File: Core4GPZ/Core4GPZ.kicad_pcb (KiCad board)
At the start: 2 copper layers, 88.9 x 114.3 mm, 20 parts, among them Q1 IRG4PF50W, Q2 IRG4PF50W, U1 core4, U2 MPX4250

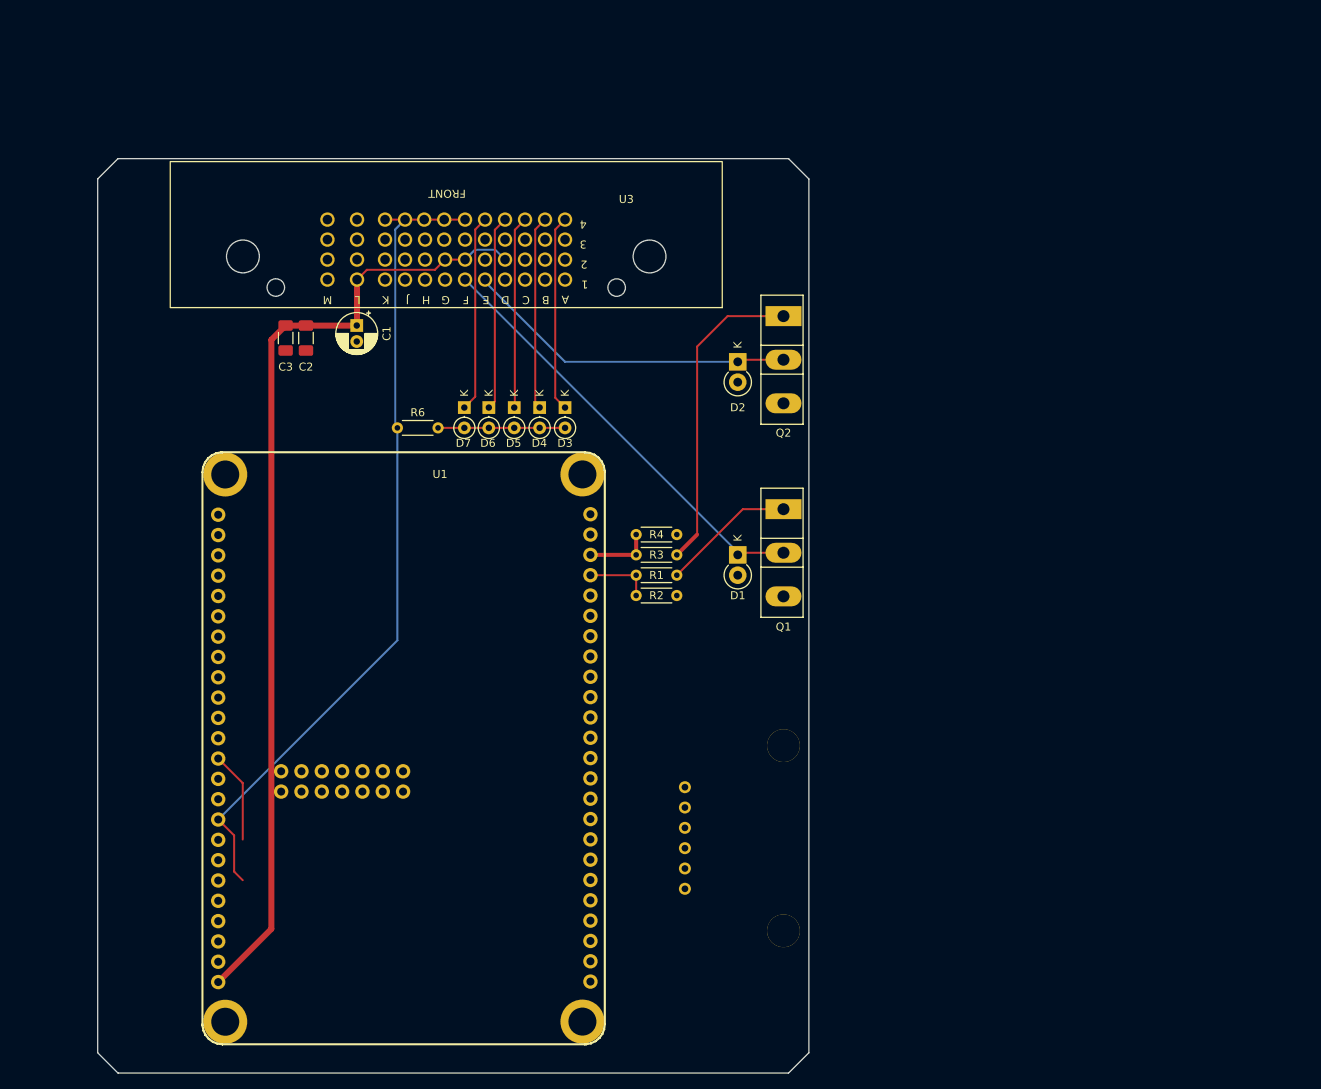
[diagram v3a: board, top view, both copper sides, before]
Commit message: Started Implementation of VR Conditionner
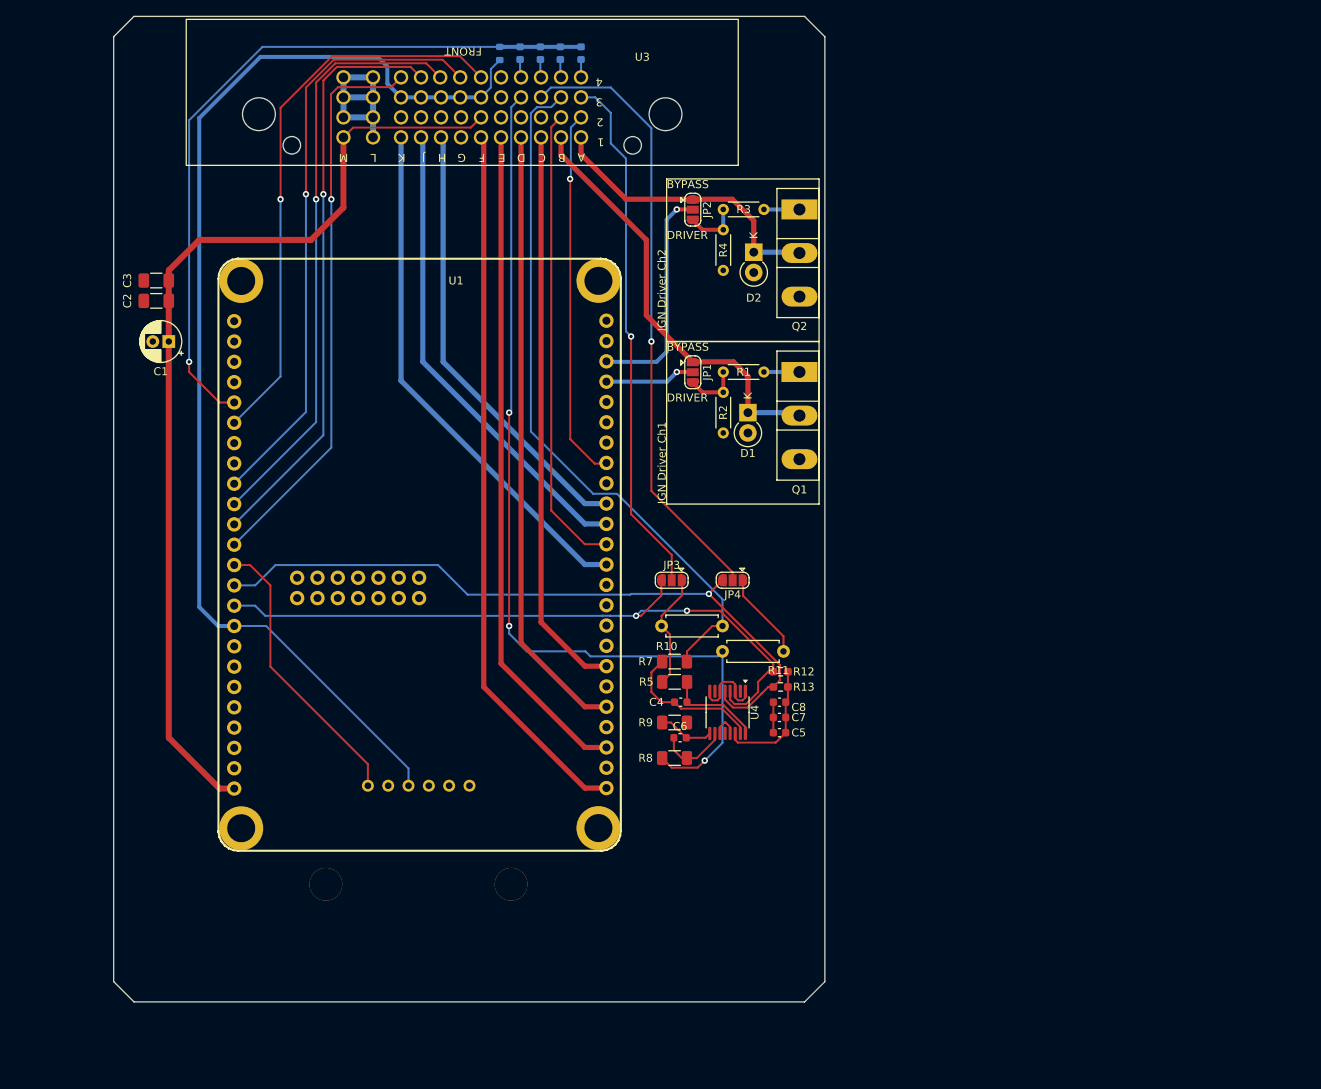
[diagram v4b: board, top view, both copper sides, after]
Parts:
- removed D7: D, Diode_THT:D_DO-35_SOD27_P2.54mm_Vertical_KathodeUp
- added C4: 1n, Capacitor_SMD:C_0603_1608Metric, F.Cu at (126.2, 108.6)
- added C5: 10n, Capacitor_SMD:C_0603_1608Metric, F.Cu at (138.6, 112.4)
- added C6: 1n, Capacitor_SMD:C_0603_1608Metric, F.Cu at (126.1, 113.0)
- added C7: 100n, Capacitor_SMD:C_0603_1608Metric, F.Cu at (138.6, 110.5)
- added C8: 1u, Capacitor_SMD:C_0603_1608Metric, F.Cu at (138.6, 108.6)
- added JP1: SolderJumper_3_Open, Jumper:SolderJumper-3_P1.3mm_Open_RoundedPad1.0x1.5mm, F.Cu at (127.7, 67.3)
- added JP2: SolderJumper_3_Open, Jumper:SolderJumper-3_P1.3mm_Open_RoundedPad1.0x1.5mm, F.Cu at (127.7, 47.0)
- added JP3: Crank - VR/Hall Selector, Jumper:SolderJumper-3_P1.3mm_Open_RoundedPad1.0x1.5mm, F.Cu at (125.1, 93.3)
- added JP4: Cam - VR/Hall Selector, Jumper:SolderJumper-3_P1.3mm_Open_RoundedPad1.0x1.5mm, F.Cu at (132.7, 93.3)
- added R10: 4.7k, Resistor_THT:R_Axial_DIN0207_L6.3mm_D2.5mm_P7.62mm_Horizontal, F.Cu at (123.8, 99.1)
- added R11: 4.7k, Resistor_THT:R_Axial_DIN0207_L6.3mm_D2.5mm_P7.62mm_Horizontal, F.Cu at (139.1, 102.2)
- added R12: 1k, Resistor_SMD:R_0603_1608Metric_Pad0.98x0.95mm_HandSolder, F.Cu at (138.7, 104.8)
- added R13: 1k, Resistor_SMD:R_0603_1608Metric_Pad0.98x0.95mm_HandSolder, F.Cu at (138.7, 106.7)
- added R5: 10k, Resistor_SMD:R_1206_3216Metric_Pad1.30x1.75mm_HandSolder, F.Cu at (125.5, 106.0)
- added R7: 10k, Resistor_SMD:R_1206_3216Metric_Pad1.30x1.75mm_HandSolder, F.Cu at (125.5, 103.5)
- added R8: 10k, Resistor_SMD:R_1206_3216Metric_Pad1.30x1.75mm_HandSolder, F.Cu at (125.5, 115.6)
- added R9: 10k, Resistor_SMD:R_1206_3216Metric_Pad1.30x1.75mm_HandSolder, F.Cu at (125.5, 111.1)
- added U4: MAX9926UAEE+, Package_SO:QSOP-16_3.9x4.9mm_P0.635mm, F.Cu at (132.1, 109.9)
- D3, D4, D5, D6: footprint Diode_THT:D_DO-35_SOD27_P2.54mm_Vertical_KathodeUp -> Diode_SMD:D_0603_1608Metric; moved to B.Cu
- R6: footprint Resistor_THT:R_Axial_DIN0204_L3.6mm_D1.6mm_P5.08mm_Horizontal -> Resistor_SMD:R_0603_1608Metric; moved to B.Cu
- moved R6 48.5 mm to (103.6, 27.5), turned to 90 degrees
- moved R3 44.5 mm to (136.6, 47.0)
- moved D6 44.5 mm to (106.1, 27.5), turned to 90 degrees
- moved D5 44.4 mm to (108.7, 27.5), turned to 90 degrees
- moved D4 44.4 mm to (111.2, 27.5), turned to 90 degrees
- moved D3 44.3 mm to (113.8, 27.5), turned to 90 degrees
- moved U2 41.7 mm to (87.1, 119.0), turned to 0 degrees
- moved R4 39.6 mm to (131.5, 49.5), turned to -90 degrees
- moved R2 27.6 mm to (131.5, 69.8), turned to -90 degrees
- moved R1 27.6 mm to (136.6, 67.3)
- moved U1 24.3 mm to (116.9, 119.3)
- moved C1 23.6 mm to (62.2, 63.5), turned to 180 degrees
- moved C2 19.3 mm to (60.7, 58.4), turned to 180 degrees
- moved U3 17.9 mm to (98.9, 22.8)
- moved D1 17.8 mm to (134.6, 72.4)
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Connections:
- R1 pad 2: IGN_TRIG_1 -> Net-(JP1-B)
- R2 pad 1: IGN_TRIG_1 -> Net-(JP1-B)
- R3 pad 2: IGN_TRIG_2 -> Net-(JP2-B)
- R4 pad 1: IGN_TRIG_2 -> Net-(JP2-B)
- U1 pad 34: /CRANK_SNSR -> CRANK_SIGNAL
- U1 pad 35: /CAM_SNSR -> CAM_SIGNAL
- U1 pad 40: /O2_SNSR -> /02_SNSR
- U1 pad 61: BIKE_+12V_SWITCHED_IN -> BIKE_GROUND
- U1 pad 62: BIKE_+12V_SWITCHED_IN -> unconnected-(U1C-+5V-Pad62)
- U3 pad 1: /INJ1_TRIG -> IGN_COIL2_DRIVE
- U3 pad 10: unconnected-(U3A-1K-Pad10) -> /IDLE_1
- U3 pad 11: BIKE_+12V_SWITCHED_IN -> /NEUTRAL_LIGHT
- U3 pad 14: BIKE_+12V_SWITCHED_IN -> unconnected-(U3A-2D-Pad14)
- U3 pad 15: /NEUTRAL_LIGHT -> unconnected-(U3A-2E-Pad15)
- U3 pad 17: BIKE_+12V_SWITCHED_IN -> unconnected-(U3A-2G-Pad17)
- U3 pad 18: /FAN_CTL -> unconnected-(U3A-2H-Pad18)
- U3 pad 19: /IDLE_1 -> unconnected-(U3A-2J-Pad19)
- U3 pad 2: /INJ2_TRIG -> IGN_COIL1_DRIVE
- U3 pad 20: /FUEL_PUMP -> unconnected-(U3A-2K-Pad20)
- U3 pad 21: /CRANK_SNSR -> CRANK_SNSR
- U3 pad 22: /CAM_SNSR -> CRANK_SNSR_VR-
- U3 pad 23: unconnected-(U3B-3C-Pad23) -> CAM_SNSR
- U3 pad 24: unconnected-(U3B-3D-Pad24) -> CAM_SNSR_VR-
- U3 pad 26: /FLEX_SNSR -> CLT_+5V
- U3 pad 27: /02_SNSR -> CLT_+5V
- U3 pad 28: /IAT_SNSR -> CLT_+5V
- U3 pad 29: /CLT_SNSR -> CLT_+5V
- U3 pad 3: /INJ3_TRIG -> /INJ4_TRIG
- U3 pad 30: /TPS_SNSR -> CLT_+5V
- U3 pad 36: CLT_+5V -> /FLEX_SNSR
- U3 pad 37: CLT_+5V -> /02_SNSR
- U3 pad 38: CLT_+5V -> /IAT_SNSR
- U3 pad 39: CLT_+5V -> /CLT_SNSR
- U3 pad 4: /INJ4_TRIG -> /INJ3_TRIG
- U3 pad 40: CLT_+5V -> /TPS_SNSR
- U3 pad 41: BIKE_+12V_SWITCHED_IN -> BIKE_GROUND
- U3 pad 42: BIKE_GROUND -> BIKE_+12V_SWITCHED_IN
- U3 pad 5: IGN_COIL2_DRIVE -> /INJ2_TRIG
- U3 pad 6: IGN_COIL1_DRIVE -> /INJ1_TRIG
- U3 pad 8: unconnected-(U3A-1H-Pad8) -> /FAN_CTL
- U3 pad 9: unconnected-(U3A-1J-Pad9) -> /FUEL_PUMP
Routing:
- net CAM_SNSR_VR-: track 0.00 -> 116.5 mm, vias 0 -> 3
- net /INJ1_TRIG: track 0.00 -> 89.4 mm
- net CAM_SIGNAL: track 0.00 -> 89.1 mm, vias 0 -> 1
- net CRANK_SNSR_VR-: track 0.00 -> 87.4 mm
- net CRANK_SIGNAL: track 0.00 -> 87.1 mm, vias 0 -> 2
- net /INJ2_TRIG: track 0.00 -> 83.6 mm
- net /INJ3_TRIG: track 0.00 -> 77.2 mm
- net CAM_SNSR: track 0.00 -> 77.1 mm, vias 0 -> 1
- net SAFE_SIGNAL: track 15.9 -> 92.0 mm, vias 0 -> 1
- net /02_SNSR: track 0.00 -> 74.9 mm, vias 0 -> 1
- net /IAT_SNSR: track 0.00 -> 74.2 mm, vias 0 -> 1
- net /CLT_SNSR: track 0.00 -> 73.6 mm, vias 0 -> 1
- net /INJ4_TRIG: track 0.00 -> 71.1 mm
- net /TPS_SNSR: track 0.00 -> 71.0 mm, vias 0 -> 1
- net /FLEX_SNSR: track 0.00 -> 70.6 mm, vias 0 -> 1
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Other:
- board size 88.9 x 114.3 mm -> 88.9 x 123.2 mm
- board text added: "BYPASS"
- board text added: "DRIVER"
- board text added: "IGN Driver Ch1"
- board text added: "IGN Driver Ch2"

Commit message: Implemented VR_Conditionner (MAX9926+)
First look at ground plane
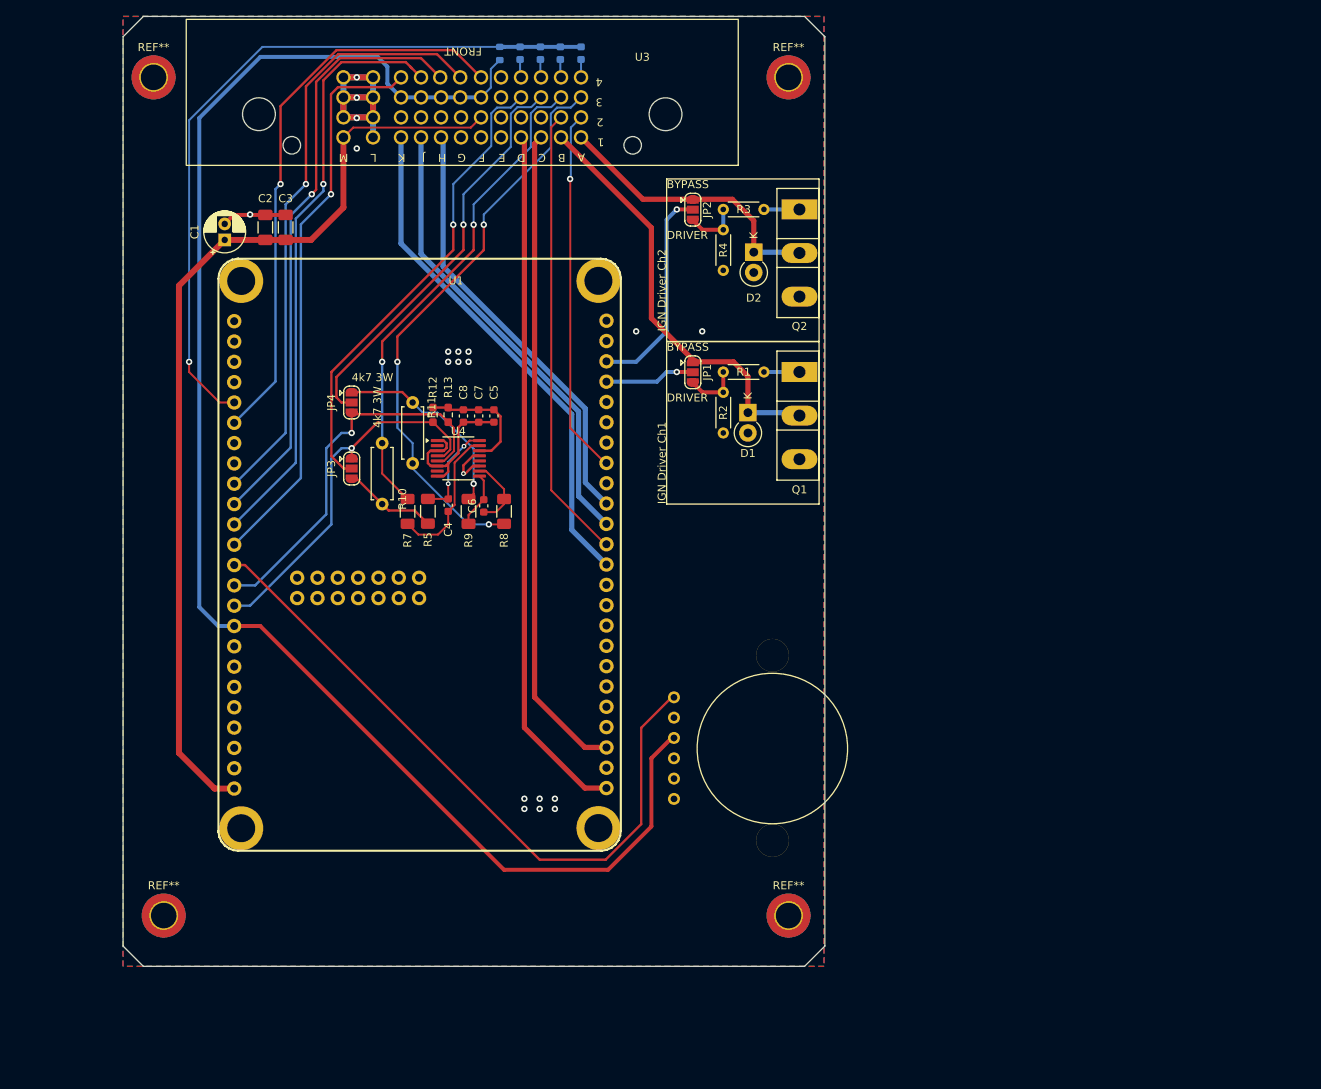
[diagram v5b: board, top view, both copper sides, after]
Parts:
- added REF**: MountingHole_3.2mm_M3_ISO14580_Pad_TopBottom, MountingHole:MountingHole_3.2mm_M3_ISO14580_Pad_TopBottom, F.Cu at (61.6, 135.3)
- added REF**: MountingHole_3.2mm_M3_ISO14580_Pad_TopBottom, MountingHole:MountingHole_3.2mm_M3_ISO14580_Pad_TopBottom, F.Cu at (139.7, 30.5)
- added REF**: MountingHole_3.2mm_M3_ISO14580_Pad_TopBottom, MountingHole:MountingHole_3.2mm_M3_ISO14580_Pad_TopBottom, F.Cu at (60.3, 30.5)
- added REF**: MountingHole_3.2mm_M3_ISO14580_Pad_TopBottom, MountingHole:MountingHole_3.2mm_M3_ISO14580_Pad_TopBottom, F.Cu at (139.7, 135.3)
- U2: moved to F.Cu
- moved R11 55.8 mm to (92.7, 71.1), turned to -90 degrees
- moved R12 54.0 mm to (95.2, 72.7), turned to -90 degrees
- moved R13 53.7 mm to (97.2, 72.7), turned to -90 degrees
- moved C5 53.3 mm to (102.9, 72.8), turned to -90 degrees
- moved C8 53.3 mm to (99.1, 72.8), turned to -90 degrees
- moved C7 53.2 mm to (101.0, 72.8), turned to -90 degrees
- moved JP4 52.6 mm to (85.1, 71.1), turned to -90 degrees
- moved U4 46.3 mm to (98.4, 78.1), turned to 0 degrees
- moved JP3 42.4 mm to (85.1, 79.4), turned to -90 degrees
- moved U2 39.8 mm to (125.4, 108.0), turned to -90 degrees
- moved R7 38.3 mm to (92.1, 84.7), turned to 90 degrees
- moved R10 38.1 mm to (88.9, 83.8), turned to 90 degrees
- moved C4 38.1 mm to (97.2, 84.0), turned to -90 degrees
- moved C6 38.0 mm to (101.6, 84.0), turned to 90 degrees
- moved R5 37.5 mm to (94.6, 84.7), turned to -90 degrees
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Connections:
- JP3 pad 1: Net-(JP3-A) -> CRANK_SIGNAL
- JP3 pad 3: CRANK_SIGNAL -> Net-(JP3-B)
- R10 pad 1: Net-(JP3-A) -> Net-(JP3-B)
- R5 pad 2: Net-(JP3-A) -> Net-(JP3-B)
- U3 pad 21: CRANK_SNSR -> CAM_SNSR_VR-
- U3 pad 24: CAM_SNSR_VR- -> CRANK_SNSR
- U3 pad 3: /INJ4_TRIG -> /INJ2_TRIG
- U3 pad 4: /INJ3_TRIG -> /INJ1_TRIG
- U3 pad 5: /INJ2_TRIG -> unconnected-(U3A-1E-Pad5)
- U3 pad 6: /INJ1_TRIG -> unconnected-(U3A-1F-Pad6)
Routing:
- net /INJ3_TRIG: track 77.2 -> 0.00 mm
- net /INJ4_TRIG: track 71.1 -> 0.00 mm
- net Net-(U1B-MAP_IN): track 35.7 -> 85.4 mm
- net CLT_+5V: track 160.7 -> 208.5 mm
- net CAM_SNSR_VR-: track 116.5 -> 72.1 mm
- net CRANK_SIGNAL: track 87.1 -> 46.7 mm, vias 2 -> 1
- net CAM_SIGNAL: track 89.1 -> 48.9 mm
- net BIKE_GROUND: track 40.9 -> 74.8 mm, vias 0 -> 20
- net CAM_SNSR: track 77.1 -> 51.3 mm
- net CRANK_SNSR_VR-: track 87.4 -> 61.8 mm, vias 0 -> 2
- net Net-(JP3-A): track 14.6 -> 0.00 mm
- net Net-(JP4-A): track 11.0 -> 24.1 mm, vias 0 -> 1
- net Net-(JP3-B): track 0.00 -> 11.8 mm
- net CRANK_SNSR: track 66.1 -> 58.9 mm
- net BIKE_+12V_SWITCHED_IN: track 121.3 -> 118.8 mm
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- added copper zone on B.Cu, net BIKE_GROUND
- added copper zone on F.Cu, net BIKE_GROUND
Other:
- board size 88.9 x 123.2 mm -> 87.7 x 118.7 mm
- board text added: "4k7 3W"

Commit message: Tiny modification
???
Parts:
- removed the REF** at (61.6, 135.3)
- removed the REF** at (139.7, 30.5)
- removed the REF** at (60.3, 30.5)
- removed the REF** at (139.7, 135.3)
- added REF**: MountingHole_3.2mm_M3_ISO14580_Pad_TopBottom, MountingHole:MountingHole_3.2mm_M3_ISO14580_Pad_TopBottom, F.Cu at (139.1, 34.9)
- added REF**: MountingHole_3.2mm_M3_ISO14580_Pad_TopBottom, MountingHole:MountingHole_3.2mm_M3_ISO14580_Pad_TopBottom, F.Cu at (59.1, 126.4)
- added REF**: MountingHole_3.2mm_M3_ISO14580_Pad_TopBottom, MountingHole:MountingHole_3.2mm_M3_ISO14580_Pad_TopBottom, F.Cu at (139.1, 126.4)
- added REF**: MountingHole_3.2mm_M3_ISO14580_Pad_TopBottom, MountingHole:MountingHole_3.2mm_M3_ISO14580_Pad_TopBottom, F.Cu at (59.1, 34.9)
- D1, D2: footprint Diode_THT:D_DO-41_SOD81_P2.54mm_Vertical_KathodeUp -> Diode_THT:D_DO-41_SOD81_P7.62mm_Horizontal
- moved U2 7.88 mm to (123.5, 100.3)
- moved D2 2.29 mm to (134.6, 50.2)
- moved D1 1.91 mm to (134.6, 70.5)
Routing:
- net Net-(U1B-MAP_IN): track 85.4 -> 56.7 mm, vias 0 -> 1
- net CLT_+5V: track 208.5 -> 234.0 mm, vias 0 -> 3
- net BIKE_GROUND: track 74.8 -> 100.2 mm, vias 20 -> 91
- net IGN_COIL2_DRIVE: track 36.0 -> 34.9 mm
- net IGN_COIL1_DRIVE: track 54.0 -> 53.1 mm
- net CAM_SIGNAL: track 48.9 -> 48.2 mm
- net /INJ2_TRIG: track 81.9 -> 81.2 mm
- net CRANK_SIGNAL: track 46.7 -> 47.3 mm
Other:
- board size 87.7 x 118.7 mm -> 90.3 x 109.2 mm
- board text added: "VR"
